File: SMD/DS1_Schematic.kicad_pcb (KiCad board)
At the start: 2 copper layers, 52.3 x 57.1 mm, 58 parts, among them J1 AudioJack3_Switch, J2 AudioJack2_Switch, J3 BAT_CON, J4 PWR_SUPP_COM, Q1 2SC2240, Q2 2SC2240, Q3 2SC2240, U1 NE5532

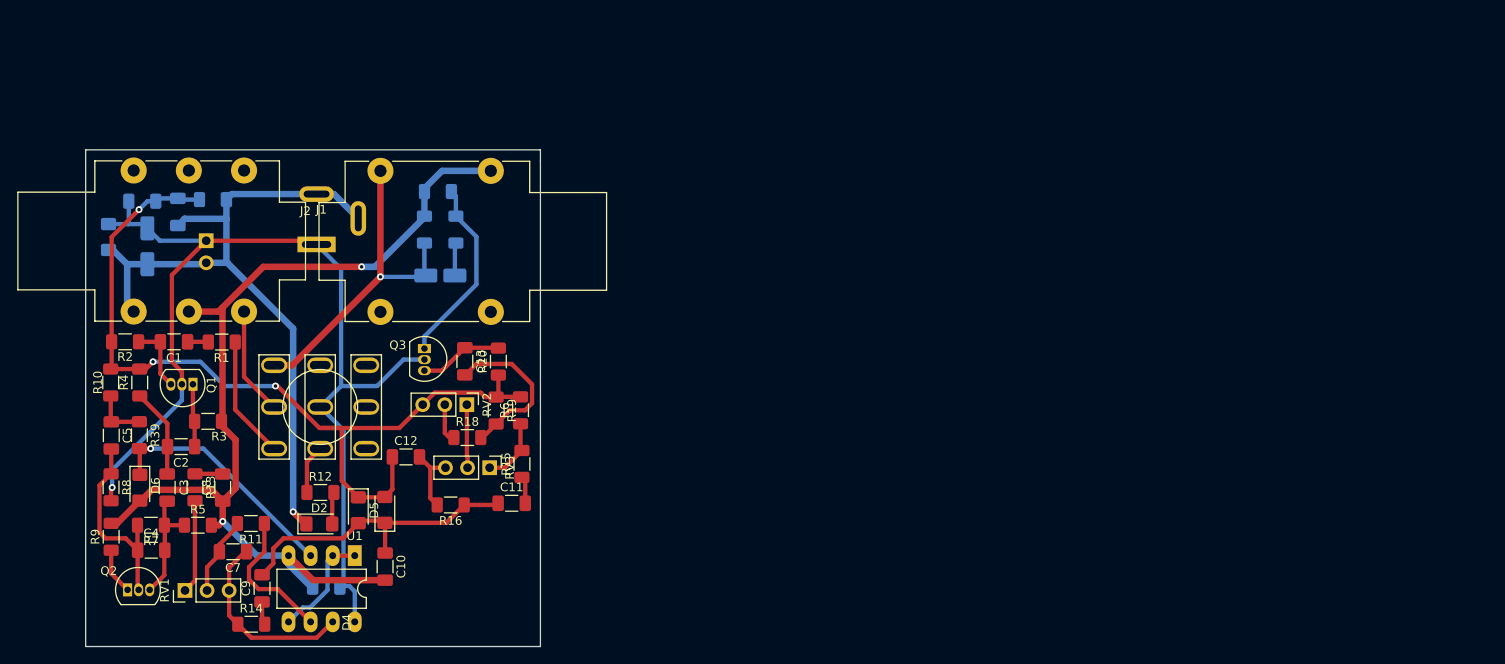
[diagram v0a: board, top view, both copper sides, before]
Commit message: new smd model
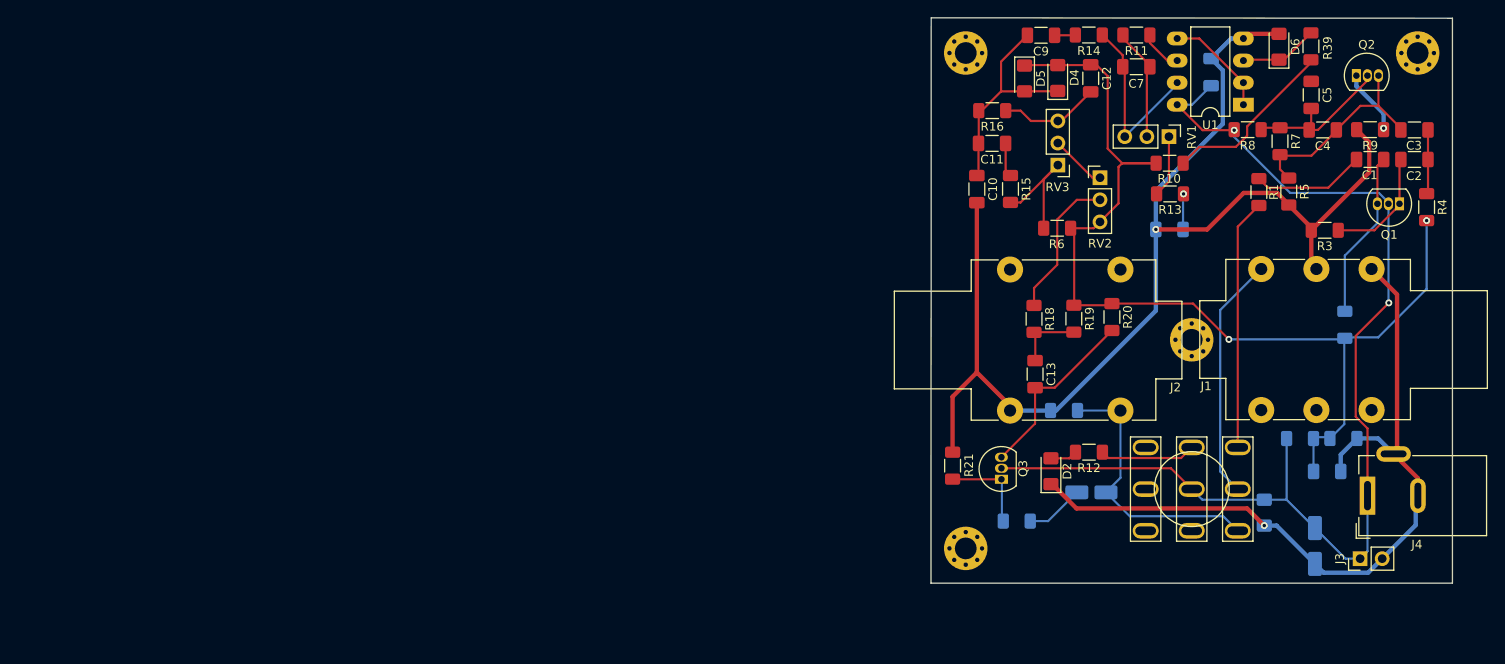
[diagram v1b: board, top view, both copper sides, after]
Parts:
- added REF**: MountingHole_2.5mm_Pad_Via, MountingHole:MountingHole_2.5mm_Pad_Via, F.Cu at (148.0, 150.0)
- added REF**: MountingHole_2.5mm_Pad_Via, MountingHole:MountingHole_2.5mm_Pad_Via, F.Cu at (174.0, 126.0)
- added REF**: MountingHole_2.5mm_Pad_Via, MountingHole:MountingHole_2.5mm_Pad_Via, F.Cu at (200.0, 93.0)
- added REF**: MountingHole_2.5mm_Pad_Via, MountingHole:MountingHole_2.5mm_Pad_Via, F.Cu at (148.0, 93.0)
- C8, R2: moved to B.Cu
- J3, J4, R21: moved to F.Cu
- moved Q2 153.3 mm to (192.9, 95.6)
- moved R9 152.2 mm to (194.5, 101.8), turned to 180 degrees
- moved R4 149.4 mm to (201.0, 110.7), turned to -90 degrees
- moved C3 149.3 mm to (199.6, 101.8), turned to 0 degrees
- moved C2 145.7 mm to (199.6, 105.2), turned to 0 degrees
- moved C5 143.5 mm to (187.7, 97.8)
- moved C4 143.2 mm to (189.1, 101.8)
- moved R39 142.0 mm to (187.7, 92.2), turned to 90 degrees
- moved D6 140.5 mm to (184.0, 92.3), turned to 90 degrees
- moved Q1 140.4 mm to (197.9, 110.3)
- moved R2 140.4 mm to (191.6, 124.3), turned to 90 degrees
- moved C1 139.2 mm to (194.5, 105.2), turned to 0 degrees
- moved C23 138.7 mm to (188.2, 149.7)
- moved J3 137.7 mm to (193.4, 151.2), turned to 90 degrees
- moved R7 137.2 mm to (184.2, 103.2), turned to 90 degrees
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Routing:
- net GND: track 111.8 -> 141.0 mm, vias 2 -> 1
- net Net-(D6-Pad1): track 27.8 -> 9.09 mm, vias 1 -> 0
- net +4.5V: track 101.5 -> 119.9 mm, vias 3 -> 2
- net Net-(J1-PadT): track 12.4 -> 28.1 mm
- net Net-(R1-Pad1): track 14.1 -> 28.8 mm
- net Net-(C5-Pad1): track 6.25 -> 20.2 mm
- net Net-(R18-Pad1): track 4.25 -> 16.9 mm
- net Net-(C13-Pad1): track 9.62 -> 21.2 mm
- net Net-(R11-Pad1): track 16.3 -> 4.88 mm
- net Net-(C1-Pad2): track 7.94 -> 19.3 mm
- net Net-(Q3-Pad1): track 21.7 -> 10.5 mm
- net Net-(C13-Pad2): track 18.7 -> 7.91 mm
- net Net-(C3-Pad1): track 13.4 -> 24.1 mm
- net Net-(C1-Pad1): track 2.40 -> 13.0 mm
- net Op-Amp Output: track 35.2 -> 25.2 mm
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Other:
- board size 52.3 x 57.1 mm -> 60 x 65 mm
